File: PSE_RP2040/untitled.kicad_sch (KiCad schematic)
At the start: 21 parts, among them U7 TPS2375-1, U8 LMR16006YQ

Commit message: MountingHole+estetica
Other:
- moved on the sheet: C31, C34
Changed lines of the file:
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@@
     (stroke (width 0) (type default) (color 0 0 0 0))
   )
-  (wire (pts (xy 152.4 45.72) (xy 152.4 62.23))
+  (wire (pts (xy 152.4 45.72) (xy 152.4 60.96))
     (stroke (width 0) (type default) (color 0 0 0 0))
   )
@@
     (stroke (width 0) (type default) (color 0 0 0 0))
   )
-  (wire (pts (xy 261.62 66.04) (xy 261.62 50.8))
+  (wire (pts (xy 261.62 53.34) (xy 261.62 50.8))
     (stroke (width 0) (type default) (color 0 0 0 0))
   )
@@
     (stroke (width 0) (type default) (color 0 0 0 0))
   )
+  (wire (pts (xy 152.4 68.58) (xy 152.4 69.85))
+    (stroke (width 0) (type default) (color 0 0 0 0))
+  )
   (wire (pts (xy 236.22 60.96) (xy 236.22 59.69))
     (stroke (width 0) (type default) (color 0 0 0 0))
   )
+  (wire (pts (xy 261.62 60.96) (xy 261.62 63.5))
+    (stroke (width 0) (type default) (color 0 0 0 0))
+  )
   (wire (pts (xy 66.04 59.69) (xy 66.04 55.88))
     (stroke (width 0) (type default) (color 0 0 0 0))
@@
     (stroke (width 0) (type default) (color 0 0 0 0))
   )
-  (wire (pts (xy 189.23 45.72) (xy 189.23 31.75))
+  (wire (pts (xy 189.23 45.72) (xy 189.23 40.64))
     (stroke (width 0) (type default) (color 0 0 0 0))
   )
@@
     (stroke (width 0) (type default) (color 0 0 0 0))
   )
+  (wire (pts (xy 271.78 63.5) (xy 271.78 60.96))
+    (stroke (width 0) (type default) (color 0 0 0 0))
+  )
   (wire (pts (xy 59.69 55.88) (xy 59.69 59.69))
     (stroke (width 0) (type default) (color 0 0 0 0))
@@
     (stroke (width 0) (type default) (color 0 0 0 0))
   )
-  (wire (pts (xy 189.23 31.75) (xy 199.39 31.75))
+  (wire (pts (xy 189.23 40.64) (xy 199.39 40.64))
     (stroke (width 0) (type default) (color 0 0 0 0))
   )
@@
   )
   (wire (pts (xy 223.52 60.96) (xy 208.28 60.96))
-    (stroke (width 0) (type default) (color 0 0 0 0))
-  )
-  (wire (pts (xy 199.39 31.75) (xy 199.39 40.64))
     (stroke (width 0) (type default) (color 0 0 0 0))
   )
@@
     (pin "1")
   )
-  (symbol (lib_id "Device:C") (at 261.62 69.85 0) (unit 1)
-    (in_bom yes) (on_board yes) (fields_autoplaced)
-    (property "Reference" "C34" (id 0) (at 264.541 69.0153 0)
-      (effects (font (size 1.27 1.27)) (justify left))
-    )
-    (property "Value" "100n" (id 1) (at 264.541 71.5522 0)
-      (effects (font (size 1.27 1.27)) (justify left))
-    )
-    (property "Footprint" "" (id 2) (at 262.5852 73.66 0)
-      (effects (font (size 1.27 1.27)) hide)
-    )
-    (property "Datasheet" "~" (id 3) (at 261.62 69.85 0)
+  (symbol (lib_id "Device:C") (at 261.62 57.15 0) (unit 1)
+    (in_bom yes) (on_board yes) (fields_autoplaced)
+    (property "Reference" "C34" (id 0) (at 264.541 56.3153 0)
+      (effects (font (size 1.27 1.27)) (justify left))
+    )
+    (property "Value" "100n" (id 1) (at 264.541 58.8522 0)
+      (effects (font (size 1.27 1.27)) (justify left))
+    )
+    (property "Footprint" "" (id 2) (at 262.5852 60.96 0)
+      (effects (font (size 1.27 1.27)) hide)
+    )
+    (property "Datasheet" "~" (id 3) (at 261.62 57.15 0)
       (effects (font (size 1.27 1.27)) hide)
     )
@@
     (pin "1")
   )
-  (symbol (lib_id "Device:C") (at 152.4 66.04 0) (unit 1)
-    (in_bom yes) (on_board yes) (fields_autoplaced)
-    (property "Reference" "C31" (id 0) (at 155.321 65.2053 0)
-      (effects (font (size 1.27 1.27)) (justify left))
-    )
-    (property "Value" "100n 100v" (id 1) (at 155.321 67.7422 0)
-      (effects (font (size 1.27 1.27)) (justify left))
-    )
-    (property "Footprint" "" (id 2) (at 153.3652 69.85 0)
-      (effects (font (size 1.27 1.27)) hide)
-    )
-    (property "Datasheet" "~" (id 3) (at 152.4 66.04 0)
-      (effects (font (size 1.27 1.27)) hide)
-    )
-    (pin "1")
-    (pin "2")
-  )
-  (symbol (lib_id "power:GND") (at 261.62 73.66 0) (unit 1)
-    (in_bom yes) (on_board yes) (fields_autoplaced)
-    (property "Reference" "#PWR0182" (id 0) (at 261.62 80.01 0)
-      (effects (font (size 1.27 1.27)) hide)
-    )
-    (property "Value" "GND" (id 1) (at 261.62 78.1034 0))
-    (property "Footprint" "" (id 2) (at 261.62 73.66 0)
-      (effects (font (size 1.27 1.27)) hide)
-    )
-    (property "Datasheet" "" (id 3) (at 261.62 73.66 0)
+  (symbol (lib_id "Device:C") (at 152.4 64.77 0) (unit 1)
+    (in_bom yes) (on_board yes) (fields_autoplaced)
+    (property "Reference" "C31" (id 0) (at 155.321 63.9353 0)
+      (effects (font (size 1.27 1.27)) (justify left))
+    )
+    (property "Value" "100n 100v" (id 1) (at 155.321 66.4722 0)
+      (effects (font (size 1.27 1.27)) (justify left))
+    )
+    (property "Footprint" "" (id 2) (at 153.3652 68.58 0)
+      (effects (font (size 1.27 1.27)) hide)
+    )
+    (property "Datasheet" "~" (id 3) (at 152.4 64.77 0)
+      (effects (font (size 1.27 1.27)) hide)
+    )
+    (pin "1")
+    (pin "2")
+  )
+  (symbol (lib_id "power:GND") (at 261.62 63.5 0) (unit 1)
+    (in_bom yes) (on_board yes) (fields_autoplaced)
+    (property "Reference" "#PWR0182" (id 0) (at 261.62 69.85 0)
+      (effects (font (size 1.27 1.27)) hide)
+    )
+    (property "Value" "GND" (id 1) (at 261.62 67.9434 0))
+    (property "Footprint" "" (id 2) (at 261.62 63.5 0)
+      (effects (font (size 1.27 1.27)) hide)
+    )
+    (property "Datasheet" "" (id 3) (at 261.62 63.5 0)
       (effects (font (size 1.27 1.27)) hide)
     )
@@
     (pin "1")
   )
-  (symbol (lib_id "power:GND") (at 271.78 60.96 0) (unit 1)
-    (in_bom yes) (on_board yes) (fields_autoplaced)
-    (property "Reference" "#PWR0184" (id 0) (at 271.78 67.31 0)
-      (effects (font (size 1.27 1.27)) hide)
-    )
-    (property "Value" "GND" (id 1) (at 271.78 65.4034 0))
-    (property "Footprint" "" (id 2) (at 271.78 60.96 0)
-      (effects (font (size 1.27 1.27)) hide)
-    )
-    (property "Datasheet" "" (id 3) (at 271.78 60.96 0)
-      (effects (font (size 1.27 1.27)) hide)
-    )
+  (symbol (lib_id "power:GND") (at 271.78 63.5 0) (unit 1)
+    (in_bom yes) (on_board yes) (fields_autoplaced)
+    (property "Reference" "#PWR0184" (id 0) (at 271.78 69.85 0)
+      (effects (font (size 1.27 1.27)) hide)
+    )
+    (property "Value" "GND" (id 1) (at 271.78 67.9434 0))
+    (property "Footprint" "" (id 2) (at 271.78 63.5 0)
+      (effects (font (size 1.27 1.27)) hide)
+    )
+    (property "Datasheet" "" (id 3) (at 271.78 63.5 0)
+      (effects (font (size 1.27 1.27)) hide)
+    )

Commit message: assegnamento footprint PAM7Q
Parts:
- C28, C31, C32, C33, C34: footprint (none) -> Capacitor_SMD:C_0603_1608Metric
- C35: footprint (none) -> Capacitor_SMD:C_0805_2012Metric
- JP1: footprint (none) -> Jumper:SolderJumper-2_P1.3mm_Bridged_Pad1.0x1.5mm
- L3: footprint (none) -> Inductor_SMD:L_0603_1608Metric
- R29, R30, R31, R32, R33, R34, R35: footprint (none) -> Resistor_SMD:R_0603_1608Metric
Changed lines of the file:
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@@
       (effects (font (size 1.27 1.27)) (justify left))
     )
-    (property "Footprint" "" (id 2) (at 221.742 55.88 90)
+    (property "Footprint" "Resistor_SMD:R_0603_1608Metric" (id 2) (at 221.742 55.88 90)
       (effects (font (size 1.27 1.27)) hide)
     )
@@
     (property "Reference" "JP1" (id 0) (at 114.3 48.26 0))
     (property "Value" "SolderJumper_2_Bridged" (id 1) (at 114.3 53.34 0))
-    (property "Footprint" "" (id 2) (at 114.3 50.8 0)
+    (property "Footprint" "Jumper:SolderJumper-2_P1.3mm_Bridged_Pad1.0x1.5mm" (id 2) (at 114.3 50.8 0)
       (effects (font (size 1.27 1.27)) hide)
     )
@@
       (effects (font (size 1.27 1.27)) (justify left))
     )
-    (property "Footprint" "" (id 2) (at 64.262 73.66 90)
+    (property "Footprint" "Resistor_SMD:R_0603_1608Metric" (id 2) (at 64.262 73.66 90)
       (effects (font (size 1.27 1.27)) hide)
     )
@@
       (effects (font (size 1.27 1.27)) (justify left))
     )
-    (property "Footprint" "" (id 2) (at 200.3552 48.26 0)
+    (property "Footprint" "Capacitor_SMD:C_0603_1608Metric" (id 2) (at 200.3552 48.26 0)
       (effects (font (size 1.27 1.27)) hide)
     )
@@
       (effects (font (size 1.27 1.27)) (justify left))
     )
-    (property "Footprint" "" (id 2) (at 221.742 66.04 90)
+    (property "Footprint" "Resistor_SMD:R_0603_1608Metric" (id 2) (at 221.742 66.04 90)
       (effects (font (size 1.27 1.27)) hide)
     )
@@
       (effects (font (size 1.27 1.27)) (justify left))
     )
-    (property "Footprint" "" (id 2) (at 57.912 52.07 90)
+    (property "Footprint" "Resistor_SMD:R_0603_1608Metric" (id 2) (at 57.912 52.07 90)
       (effects (font (size 1.27 1.27)) hide)
     )
@@
       (effects (font (size 1.27 1.27)) (justify left))
     )
-    (property "Footprint" "" (id 2) (at 272.7452 60.96 0)
+    (property "Footprint" "Capacitor_SMD:C_0805_2012Metric" (id 2) (at 272.7452 60.96 0)
       (effects (font (size 1.27 1.27)) hide)
     )
@@
       (effects (font (size 1.27 1.27)) (justify left))
     )
-    (property "Footprint" "" (id 2) (at 262.5852 60.96 0)
+    (property "Footprint" "Capacitor_SMD:C_0603_1608Metric" (id 2) (at 262.5852 60.96 0)
       (effects (font (size 1.27 1.27)) hide)
     )
@@
       (effects (font (size 1.27 1.27)) (justify left))
     )
-    (property "Footprint" "" (id 2) (at 153.3652 68.58 0)
+    (property "Footprint" "Capacitor_SMD:C_0603_1608Metric" (id 2) (at 153.3652 68.58 0)
       (effects (font (size 1.27 1.27)) hide)
     )
@@
       (effects (font (size 1.27 1.27)) (justify left))
     )
-    (property "Footprint" "" (id 2) (at 237.1852 59.69 0)
+    (property "Footprint" "Capacitor_SMD:C_0603_1608Metric" (id 2) (at 237.1852 59.69 0)
       (effects (font (size 1.27 1.27)) hide)
     )
@@
       (effects (font (size 1.27 1.27)) (justify left))
     )
-    (property "Footprint" "" (id 2) (at 64.262 52.07 90)
+    (property "Footprint" "Resistor_SMD:R_0603_1608Metric" (id 2) (at 64.262 52.07 90)
       (effects (font (size 1.27 1.27)) hide)
     )
@@
     (property "Reference" "L3" (id 0) (at 212.09 46.5922 90))
     (property "Value" "L" (id 1) (at 212.09 49.1291 90))
-    (property "Footprint" "" (id 2) (at 212.09 50.8 0)
+    (property "Footprint" "Inductor_SMD:L_0603_1608Metric" (id 2) (at 212.09 50.8 0)
       (effects (font (size 1.27 1.27)) hide)
     )
@@
       (effects (font (size 1.27 1.27)) (justify left))
     )
-    (property "Footprint" "" (id 2) (at 64.262 83.82 90)
+    (property "Footprint" "Resistor_SMD:R_0603_1608Metric" (id 2) (at 64.262 83.82 90)
       (effects (font (size 1.27 1.27)) hide)
     )
@@
       (effects (font (size 1.27 1.27)) (justify left))
     )
-    (property "Footprint" "" (id 2) (at 47.9552 62.23 0)
+    (property "Footprint" "Capacitor_SMD:C_0603_1608Metric" (id 2) (at 47.9552 62.23 0)
       (effects (font (size 1.27 1.27)) hide)
     )
@@
       (effects (font (size 1.27 1.27)) (justify left))
     )
-    (property "Footprint" "" (id 2) (at 57.912 73.66 90)
-      (effects (font (size 1.27 1.27)) hide)
-    )
+    (property "Footprint" "Resistor_SMD:R_0603_1608Metric" (id 2) (at 57.912 73.66 90)
+      (effects (font (size 1.27 1.27)) hide)
+    )

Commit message: footprint, aggiunto bottone rst
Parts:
- removed D6: MBR1020VL, Diode_SMD:D_SOD-123F, symbol Diode:MBR1020VL
- added D6: (no value), symbol Device:D_Schottky
- L3: value L -> (none); footprint Inductor_SMD:L_0603_1608Metric -> (none)
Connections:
- net GND: now also D6.2 (A)
- net at C32.2, L3.1, U8.6 (SW): now also D6.1 (K)
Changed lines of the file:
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@@
     (stroke (width 0) (type default) (color 0 0 0 0))
   )
-  (wire (pts (xy 199.39 50.8) (xy 199.39 53.34))
+  (wire (pts (xy 199.39 50.8) (xy 199.39 62.23))
     (stroke (width 0) (type default) (color 0 0 0 0))
   )
@@
     )
     (property "Datasheet" "~" (id 3) (at 271.78 57.15 0)
-      (effects (font (size 1.27 1.27)) hide)
-    )
-    (pin "1")
-    (pin "2")
-  )
-  (symbol (lib_id "Diode:MBR1020VL") (at 199.39 57.15 270) (unit 1)
-    (in_bom yes) (on_board yes)
-    (property "Reference" "D6" (id 0) (at 193.9036 57.15 0))
-    (property "Value" "MBR1020VL" (id 1) (at 196.215 57.15 0))
-    (property "Footprint" "Diode_SMD:D_SOD-123F" (id 2) (at 194.945 57.15 0)
-      (effects (font (size 1.27 1.27)) hide)
-    )
-    (property "Datasheet" "https://www.onsemi.com/pub/Collateral/MBR1020VL-D.PDF" (id 3) (at 199.39 57.15 0)
       (effects (font (size 1.27 1.27)) hide)
     )
@@
     (pin "1")
   )
-  (symbol (lib_id "power:GND") (at 199.39 60.96 0) (unit 1)
-    (in_bom yes) (on_board yes) (fields_autoplaced)
-    (property "Reference" "#PWR0186" (id 0) (at 199.39 67.31 0)
-      (effects (font (size 1.27 1.27)) hide)
-    )
-    (property "Value" "GND" (id 1) (at 199.39 65.4034 0))
-    (property "Footprint" "" (id 2) (at 199.39 60.96 0)
-      (effects (font (size 1.27 1.27)) hide)
-    )
-    (property "Datasheet" "" (id 3) (at 199.39 60.96 0)
+  (symbol (lib_id "power:GND") (at 199.39 69.85 0) (unit 1)
+    (in_bom yes) (on_board yes) (fields_autoplaced)
+    (property "Reference" "#PWR0186" (id 0) (at 199.39 76.2 0)
+      (effects (font (size 1.27 1.27)) hide)
+    )
+    (property "Value" "GND" (id 1) (at 199.39 74.2934 0))
+    (property "Footprint" "" (id 2) (at 199.39 69.85 0)
+      (effects (font (size 1.27 1.27)) hide)
+    )
+    (property "Datasheet" "" (id 3) (at 199.39 69.85 0)
       (effects (font (size 1.27 1.27)) hide)
     )
@@
     (pin "1")
   )
+  (symbol (lib_id "Device:D_Schottky") (at 199.39 66.04 270) (unit 1)
+    (in_bom yes) (on_board yes) (fields_autoplaced)
+    (property "Reference" "D6" (id 0) (at 201.93 64.4524 90)
+      (effects (font (size 1.27 1.27)) (justify left))
+    )
+    (property "Value" "" (id 1) (at 201.93 66.9924 90)
+      (effects (font (size 1.27 1.27)) (justify left))
+    )
+    (property "Footprint" "" (id 2) (at 199.39 66.04 0)
+      (effects (font (size 1.27 1.27)) hide)
+    )
+    (property "Datasheet" "~" (id 3) (at 199.39 66.04 0)
+      (effects (font (size 1.27 1.27)) hide)
+    )
+    (pin "1")
+    (pin "2")
+  )
   (symbol (lib_id "Device:C") (at 152.4 64.77 0) (unit 1)
     (in_bom yes) (on_board yes) (fields_autoplaced)
@@
     (in_bom yes) (on_board yes) (fields_autoplaced)
     (property "Reference" "L3" (id 0) (at 212.09 46.5922 90))
-    (property "Value" "L" (id 1) (at 212.09 49.1291 90))
-    (property "Footprint" "Inductor_SMD:L_0603_1608Metric" (id 2) (at 212.09 50.8 0)
-      (effects (font (size 1.27 1.27)) hide)
-    )
+    (property "Value" "" (id 1) (at 212.09 49.1291 90))
+    (property "Footprint" "" (id 2) (at 212.09 50.8 0)
+      (effects (font (size 1.27 1.27)) hide)
+    )

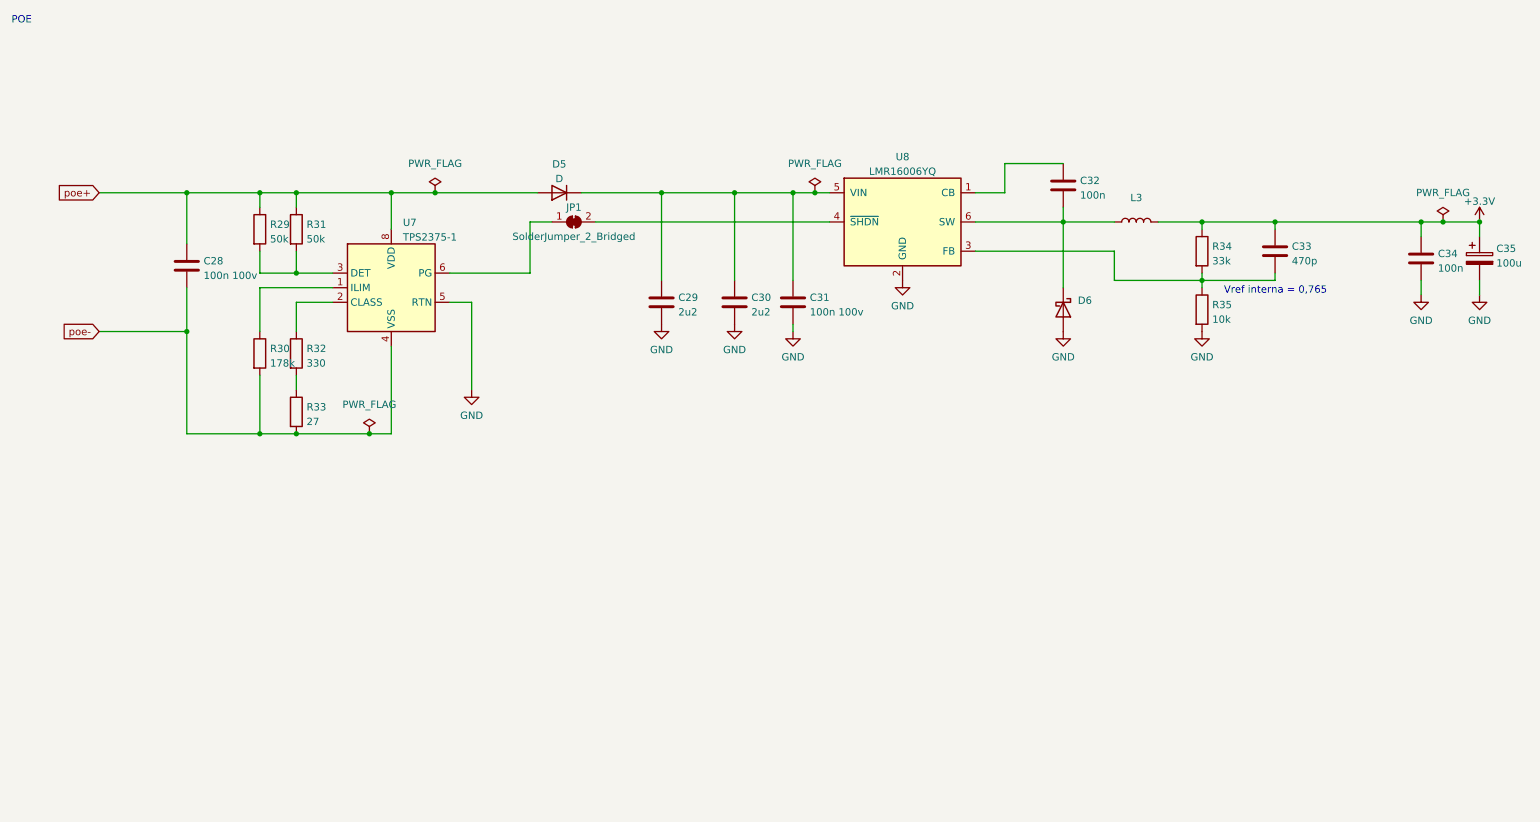
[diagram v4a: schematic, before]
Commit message: OR a diodi, connettore ext PoE
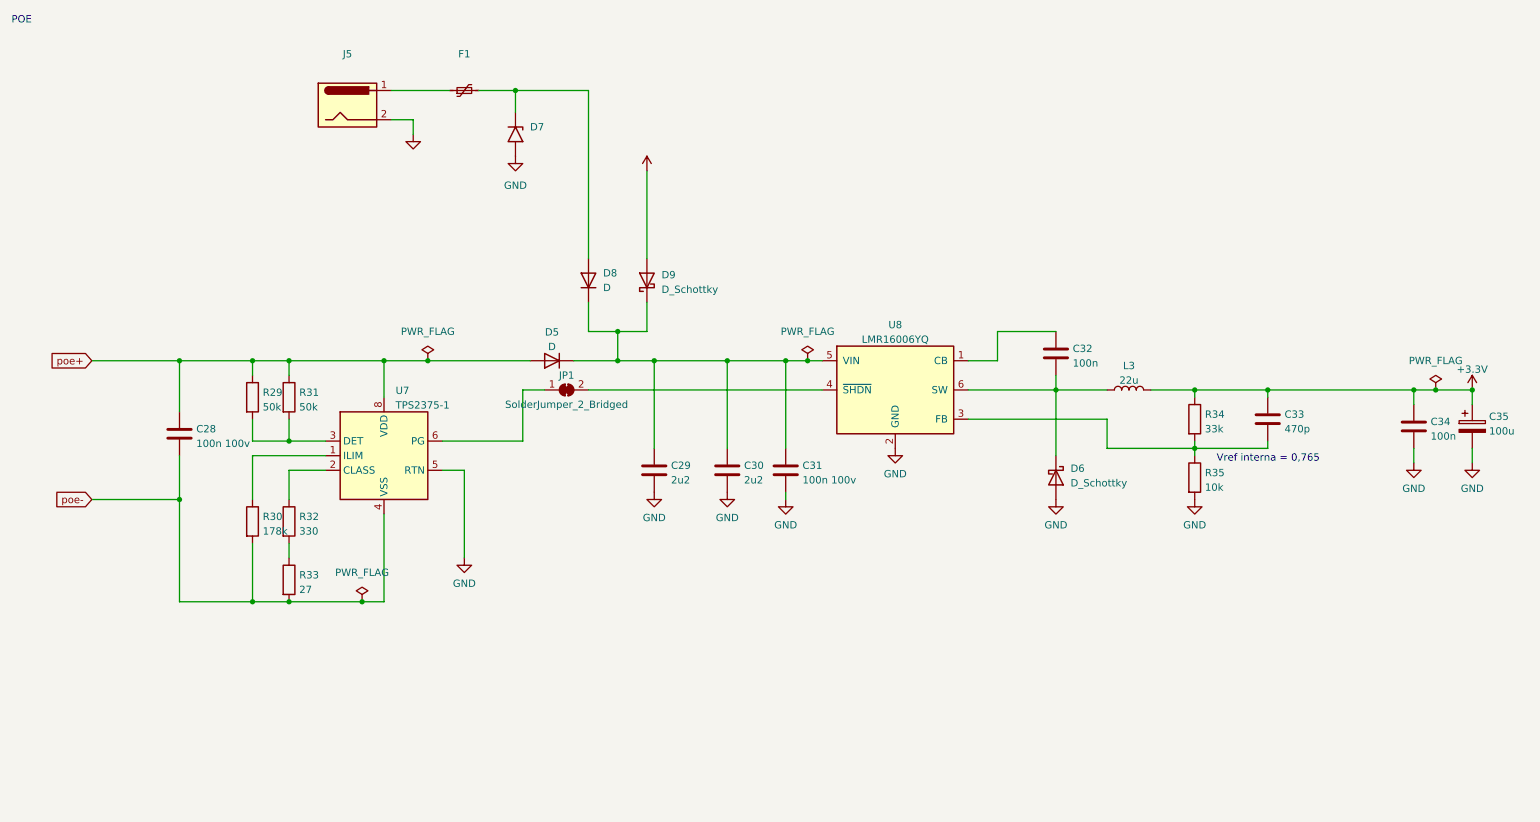
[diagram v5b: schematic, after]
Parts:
- added D7: (no value), symbol Diode:1.5KExxA
- added D8: D, symbol Device:D
- added D9: D_Schottky, Diode_SMD:D_SMA, symbol Device:D_Schottky
- added F1: (no value), symbol Device:Polyfuse_Small
- added J5: (no value), symbol Connector:Barrel_Jack
- D6: value (none) -> D_Schottky; footprint (none) -> Diode_SMD:D_SMA
- L3: value (none) -> 22u; footprint (none) -> Inductor_SMD:L_6.3x6.3_H3
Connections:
- net GND: now also D7.2 (A2), J5.2
- net at C29.1, C30.1, C31.1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: now also D8.1 (K), D9.1 (K)
- new net: D7.1 (A1), D8.2 (A), F1.2
- new net: F1.1, J5.1
- new net +5V: D9.2 (A)
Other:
- moved on the sheet: C28, C29, C30, C31, C32, C33, C34, C35, D5, D6, JP1, L3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

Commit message: valore resistenze lan
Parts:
- D7: value (none) -> 1.5KExxA; footprint (none) -> Diode_THT:D_DO-201AE_P15.24mm_Horizontal
- F1: value (none) -> Polyfuse_Small
- J5: value (none) -> Barrel_Jack
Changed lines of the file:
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@@
       (effects (font (size 1.27 1.27)) hide)
     )
-    (property "Value" "" (id 1) (at 86.36 40.64 0))
+    (property "Value" "GND" (id 1) (at 86.36 40.64 0))
     (property "Footprint" "" (id 2) (at 86.36 35.56 0)
       (effects (font (size 1.27 1.27)) hide)
@@
     (in_bom yes) (on_board yes) (fields_autoplaced)
     (property "Reference" "F1" (id 0) (at 95.25 21.59 90))
-    (property "Value" "" (id 1) (at 95.25 24.13 90))
+    (property "Value" "Polyfuse_Small" (id 1) (at 95.25 24.13 90))
     (property "Footprint" "" (id 2) (at 100.33 26.67 0)
       (effects (font (size 1.27 1.27)) (justify left) hide)
@@
       (effects (font (size 1.27 1.27)) (justify left))
     )
-    (property "Value" "" (id 1) (at 106.68 36.8299 90)
-      (effects (font (size 1.27 1.27)) (justify left))
-    )
-    (property "Footprint" "" (id 2) (at 99.06 35.56 0)
+    (property "Value" "1.5KExxA" (id 1) (at 106.68 36.8299 90)
+      (effects (font (size 1.27 1.27)) (justify left))
+    )
+    (property "Footprint" "Diode_THT:D_DO-201AE_P15.24mm_Horizontal" (id 2) (at 99.06 35.56 0)
       (effects (font (size 1.27 1.27)) hide)
     )
@@
       (effects (font (size 1.27 1.27)) hide)
     )
-    (property "Value" "" (id 1) (at 127 36.83 0))
+    (property "Value" "+5V" (id 1) (at 127 36.83 0))
     (property "Footprint" "" (id 2) (at 127 41.91 0)
       (effects (font (size 1.27 1.27)) hide)
@@
     (in_bom yes) (on_board yes) (fields_autoplaced)
     (property "Reference" "J5" (id 0) (at 74.93 21.59 0))
-    (property "Value" "" (id 1) (at 74.93 24.13 0))
+    (property "Value" "Barrel_Jack" (id 1) (at 74.93 24.13 0))
     (property "Footprint" "" (id 2) (at 76.2 31.496 0)
       (effects (font (size 1.27 1.27)) hide)
